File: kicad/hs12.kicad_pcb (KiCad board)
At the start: 2 copper layers, 62.6 x 42.7 mm, 200 parts, among them J1 Spacer M2, J2 Spacer M2, J3 Screw M2, J4 Screw M2, J5 Screw M2, J6 Screw M2

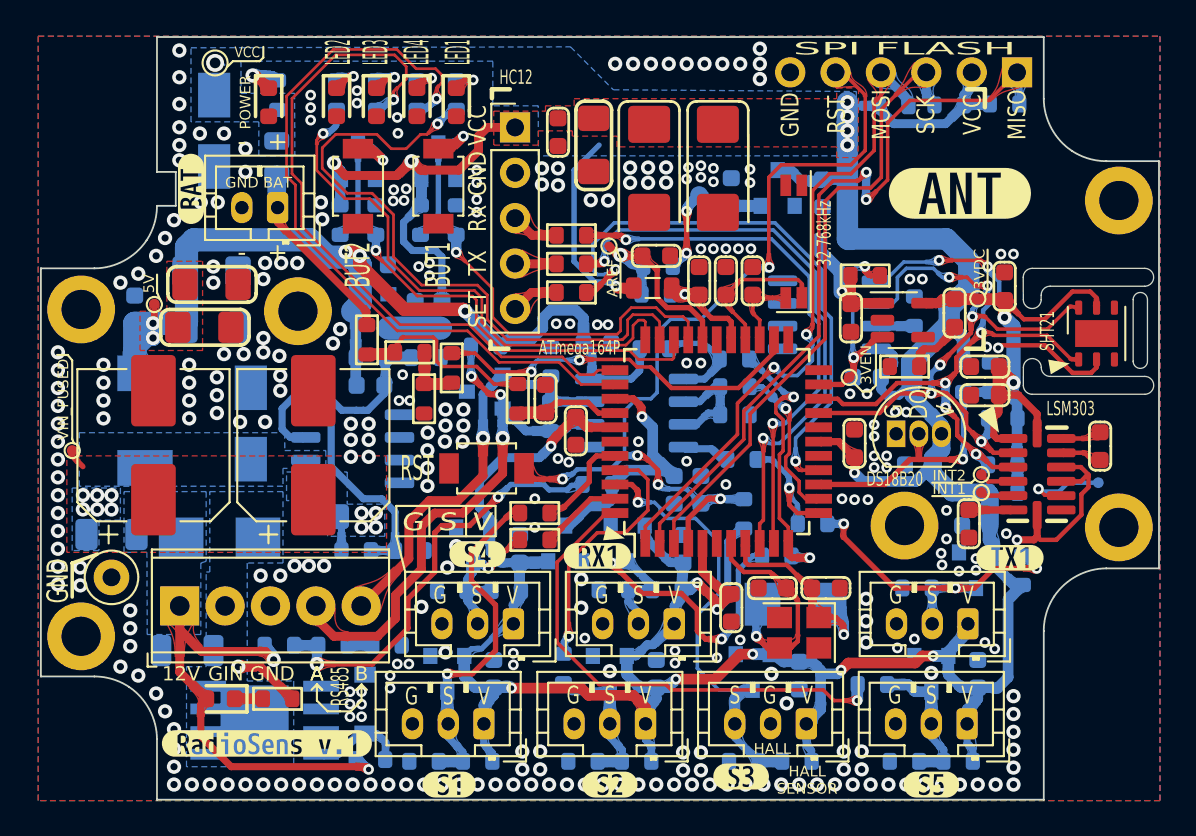
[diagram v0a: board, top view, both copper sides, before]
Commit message: Reannotate schematic; Fix 5032 crystal footprint field; Update PCB with 5032 crystal
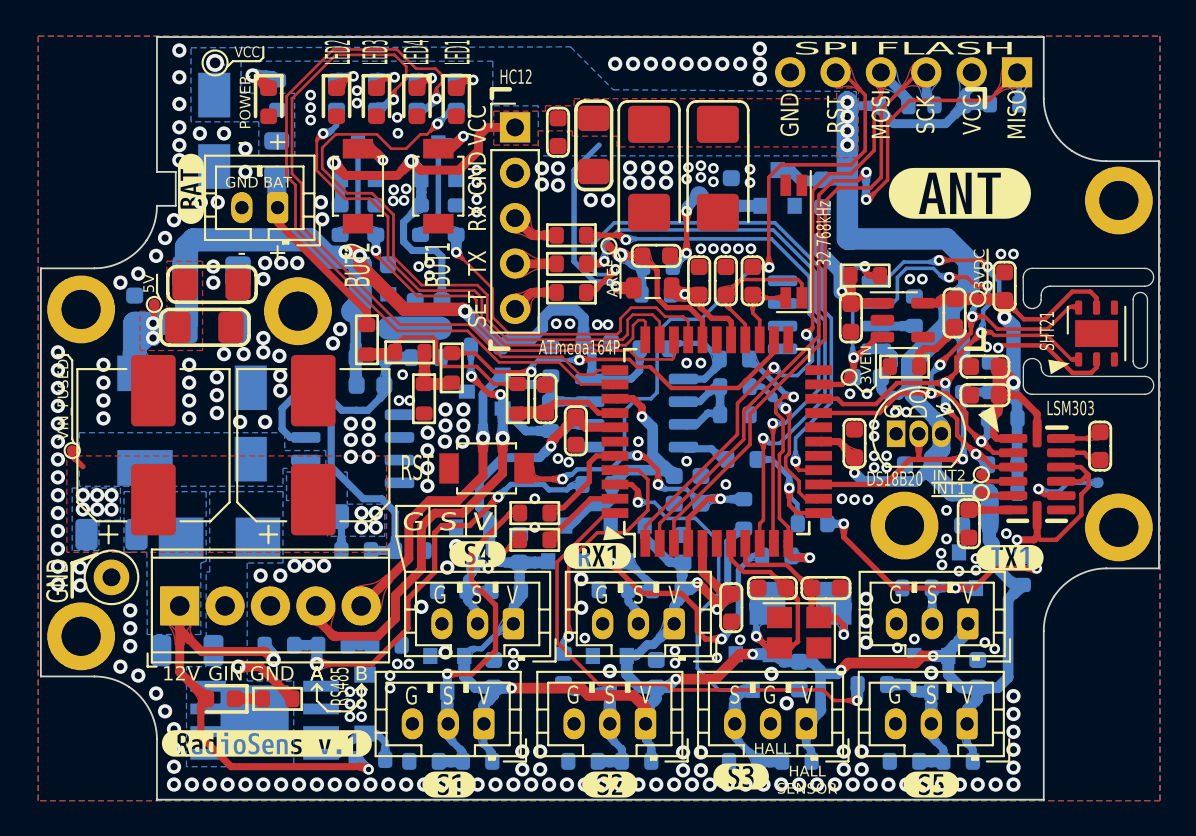
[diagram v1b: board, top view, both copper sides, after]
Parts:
- removed the BQ2 at (111.0, 110.4)
- added BQ3: 5032 8MHz, Crystal:Crystal_SMD_5032-2Pin_5.0x3.2mm, B.Cu at (111.3, 110.4)
- renumbered BQ3 to BQ1, BQ1 to BQ2, C11 to C1, C35 to C10, C30 to C11, C32 to C12, C33 to C13, C9 to C14, C7 to C15, C22 to C16, C13 to C17, C23 to C18, C25 to C19, C12 to C2, C15 to C20, C18 to C21, C16 to C22, C17 to C23, C19 to C24, C20 to C25, C45 to C26, C4 to C27, C1 to C28, C2 to C29, C44 to C3, C8 to C30, C5 to C31, C6 to C32, C46 to C33, C47 to C34, C37 to C35, C26 to C36, C38 to C37, C39 to C38, C40 to C39, C41 to C4, C36 to C40, C27 to C41, C28 to C42, C3 to C43, C31 to C44, C14 to C45, C24 to C46, C42 to C5, C34 to C6, C10 to C7, C29 to C8, C21 to C9, DA4 to DA1, DA1 to DA3, DA5 to DA4, DA3 to DA5, DD3 to DD1, DD1 to DD2, DD2 to DD3, DD5 to DD4, DD4 to DD5, HL3 to HL1, HL4 to HL2, HL1 to HL3, HL5 to HL4, HL6 to HL5, HL2 to HL6, L2 to L1, L1 to L2, R33 to R1, R16 to R10, R17 to R11, R18 to R12, R19 to R13, R20 to R14, R68 to R15, R66 to R16, R67 to R17, R62 to R18, R35 to R19, R34 to R2, R36 to R20, R23 to R22, R24 to R23, R45 to R24, R49 to R25, R69 to R26, R37 to R27, R26 to R28, R9 to R29, R65 to R3, R27 to R30, R28 to R31, R29 to R32, R50 to R33, R51 to R34, R70 to R35, R47 to R36, R48 to R37, R52 to R38, R53 to R39, R10 to R4, R71 to R40, R56 to R41, R57 to R42, R72 to R43, R58 to R44, R59 to R45, R73 to R46, R60 to R47, R61 to R48, R64 to R49, R11 to R5, R38 to R50, R41 to R51, R42 to R52, R43 to R53, R25 to R54, R4 to R55, R3 to R56, R6 to R57, R7 to R58, R39 to R59, R13 to R6, R40 to R60, R5 to R61, R8 to R62, R22 to R63, R44 to R64, R2 to R65, R30 to R66, R31 to R67, R32 to R68, R54 to R69, R12 to R7, R55 to R70, R63 to R71, R46 to R72, R14 to R8, R15 to R9, SB3 to SB2, SB2 to SB3, VD6 to VD1, VD16 to VD10, VD4 to VD11, VD3 to VD12, VD2 to VD13, VD1 to VD14, VD12 to VD15, VD7 to VD2, VD8 to VD3, VD5 to VD4, VD11 to VD5, VD9 to VD6, VD10 to VD7, VD13 to VD8, VD15 to VD9, XB8 to XB1, XB12 to XB10, XB7 to XB11, XB6 to XB12, XB3 to XB2, XB1 to XB3, XB2 to XB4, XB4 to XB5, XB9 to XB6, XB5 to XB7, XB10 to XB8, XB11 to XB9, XT2 to XT1, XT4 to XT10, XT6 to XT2, XT1 to XT3, XT10 to XT4, XT3 to XT5, XT13 to XT6, XT15 to XT7, XT16 to XT8
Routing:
- net XTAL1: track 11.3 -> 12.5 mm
